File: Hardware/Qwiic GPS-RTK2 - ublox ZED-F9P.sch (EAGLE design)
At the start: 68 parts, among them J1 Radio, J13 U.FL, J3 PTH, U2 3.3V, U3 ZED-F9P

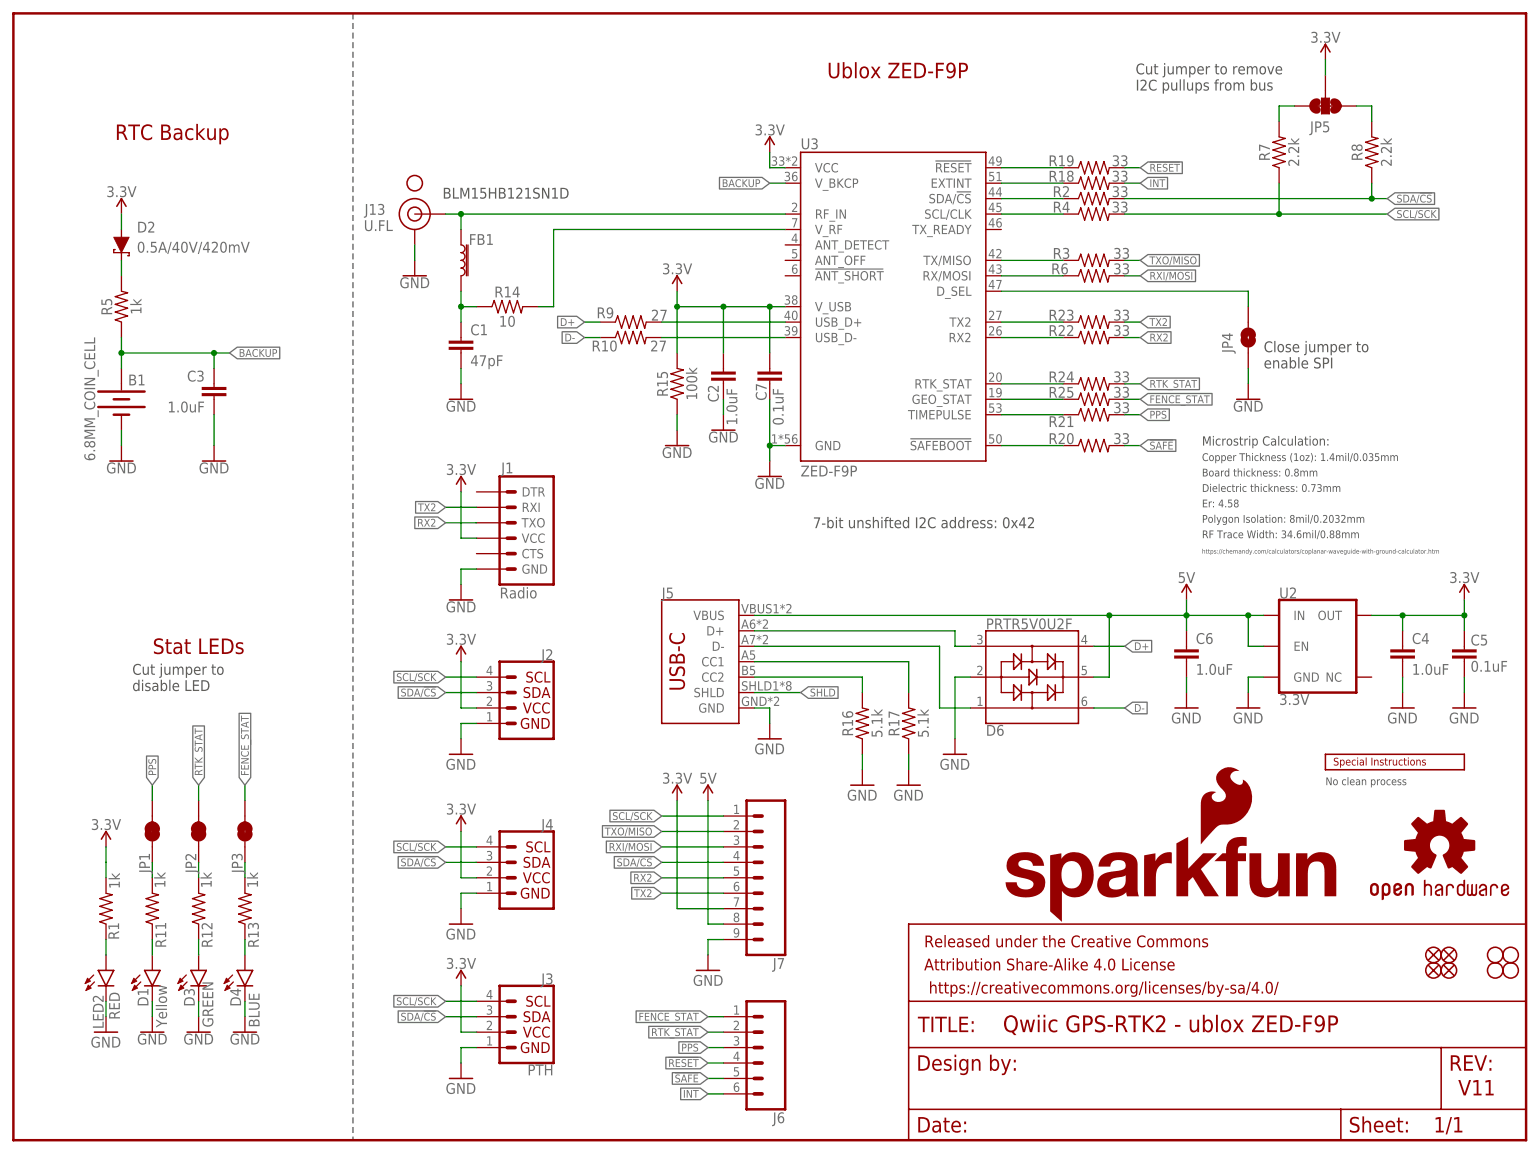
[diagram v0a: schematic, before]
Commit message: Adds reflowable battery and uses all parts from SparkFun Libraries
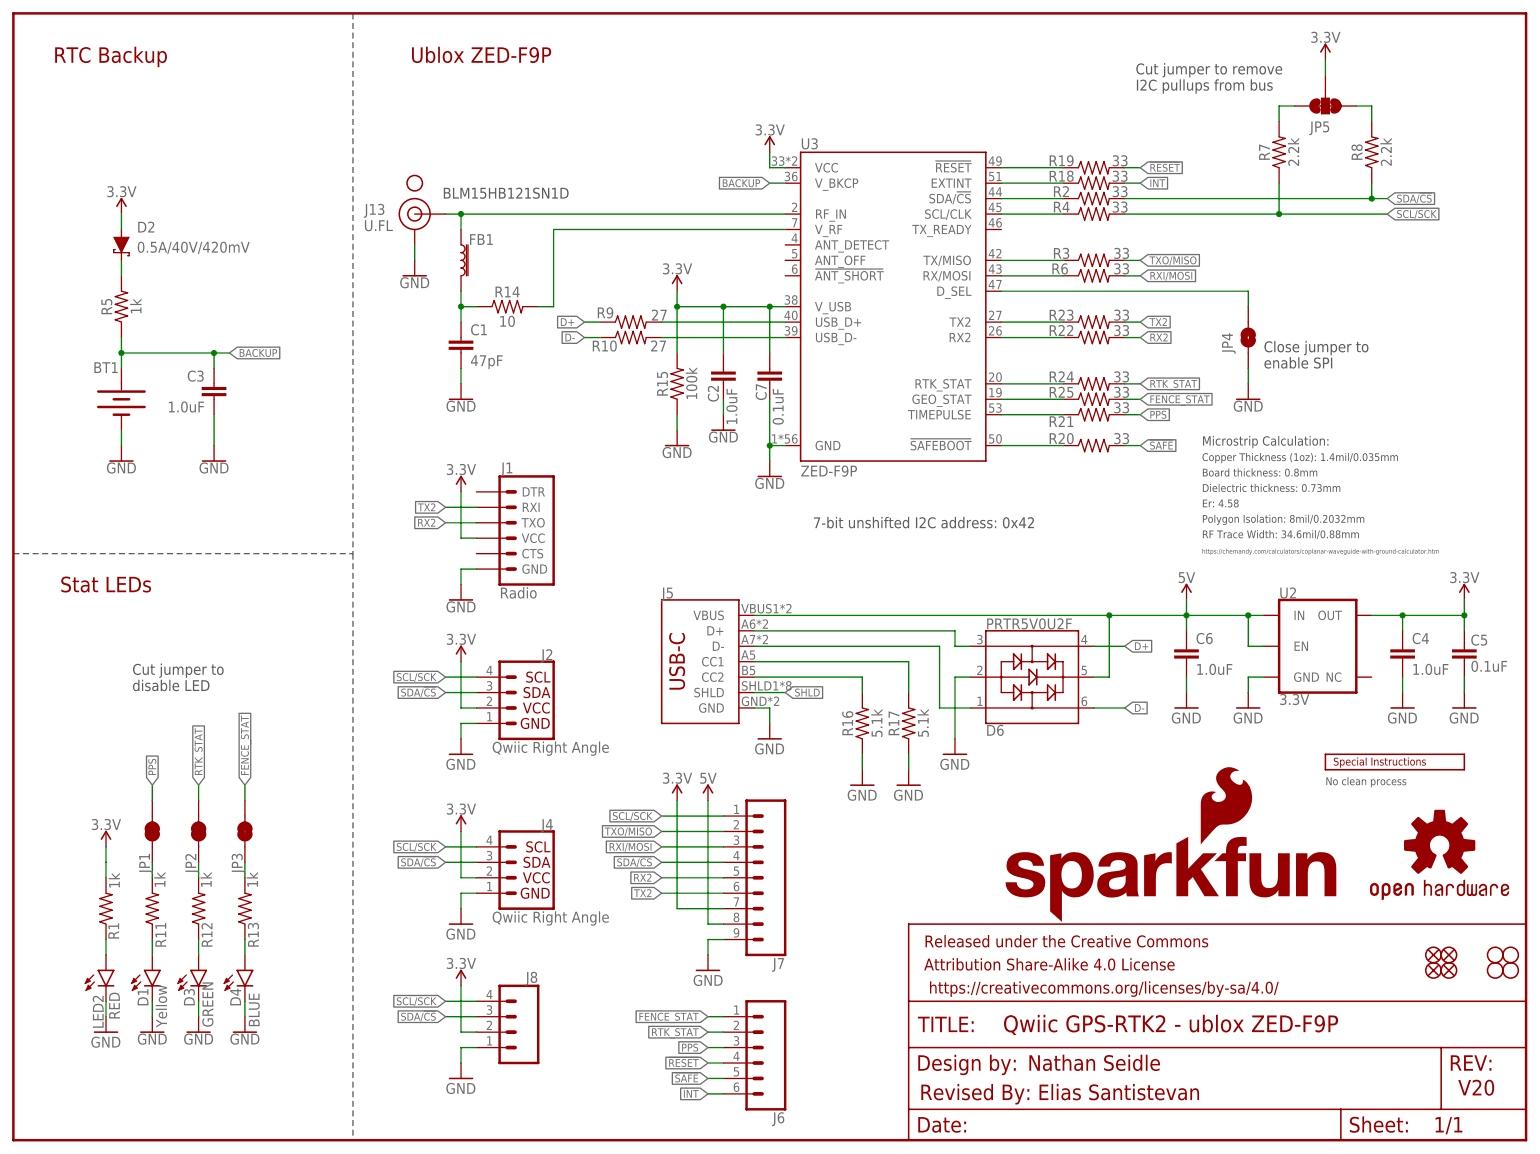
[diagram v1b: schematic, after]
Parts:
- removed B1: 6.8MM_COIN_CELL, SparkFun-Batteries:BATTERY-6.8MM_SMD
- removed J3: PTH, SparkX:I2C_STANDARD_NO_SILK
- added BT1: ML414H_IV01E_BATTERY, SparkFun-Batteries:ML414H_IV01E_BATTERY
- added J8: (no value), SparkFun-Connectors:CONN_041X04_NO_SILK
- J2, J4: value (none) -> Qwiic Right Angle
- J5: device SparkFun-Connectors:USB_C16PIN -> SparkFun-Connectors:USB_C2-LAYER
- JP101, JP31, JP41, JP91: value STAND-OFF -> STAND-OFFTIGHT; device SparkFun:STAND-OFF -> SparkFun-Hardware:STAND-OFFTIGHT
- JP21, JP61, JP71, JP81: device SparkFun:FIDUCIALUFIDUCIAL -> SparkFun-Aesthetics:FIDUCIALUFIDUCIAL
- U3: device ZED-F9P:ZED-F9P -> SparkFun-GPS:ZED-F9P
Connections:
- net 3.3V: now also J8.2; no longer J3.VCC
- net BACKUP: now also BT1.+; no longer B1.+
- net GND: now also BT1.-, J8.1; no longer B1.-, J3.GND
- net SCL/SCK: now also J8.4; no longer J3.SCL
- net SDA/!CS: now also J8.3; no longer J3.SDA
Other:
- note added: "Nathan Seidle"
- note added: "Revised By: Elias Santistevan"
- note added: "V20"
- note removed: "V11"
